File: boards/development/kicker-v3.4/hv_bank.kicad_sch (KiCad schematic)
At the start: 14 parts, among them Q3 BSS127S, Q4 AOD1N60

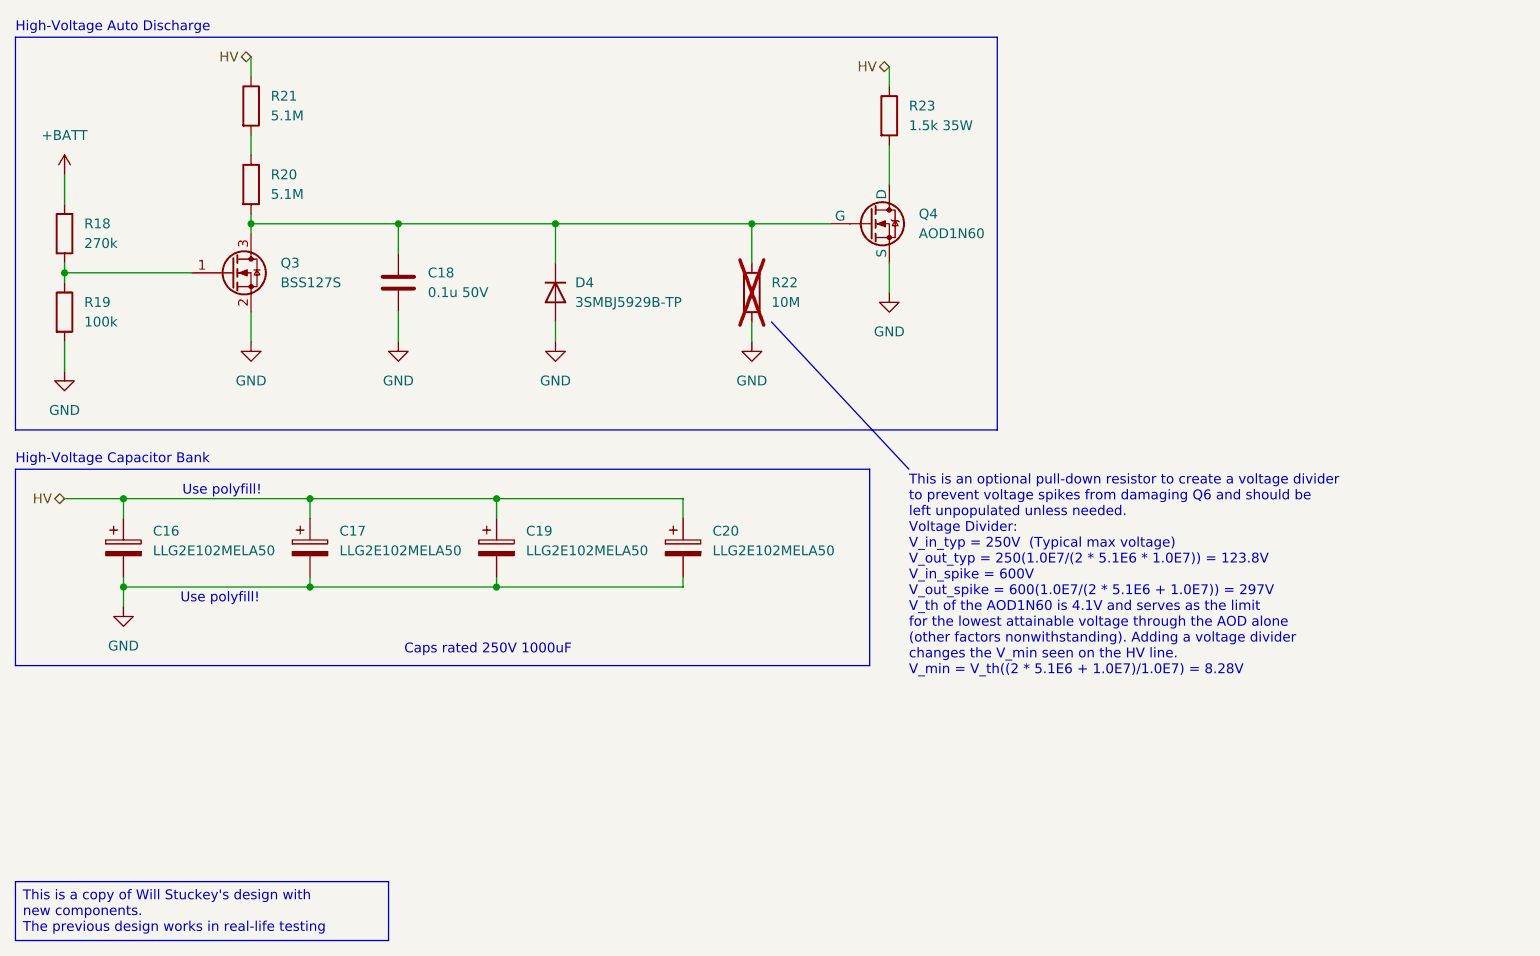
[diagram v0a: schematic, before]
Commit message: Add high voltage discharge
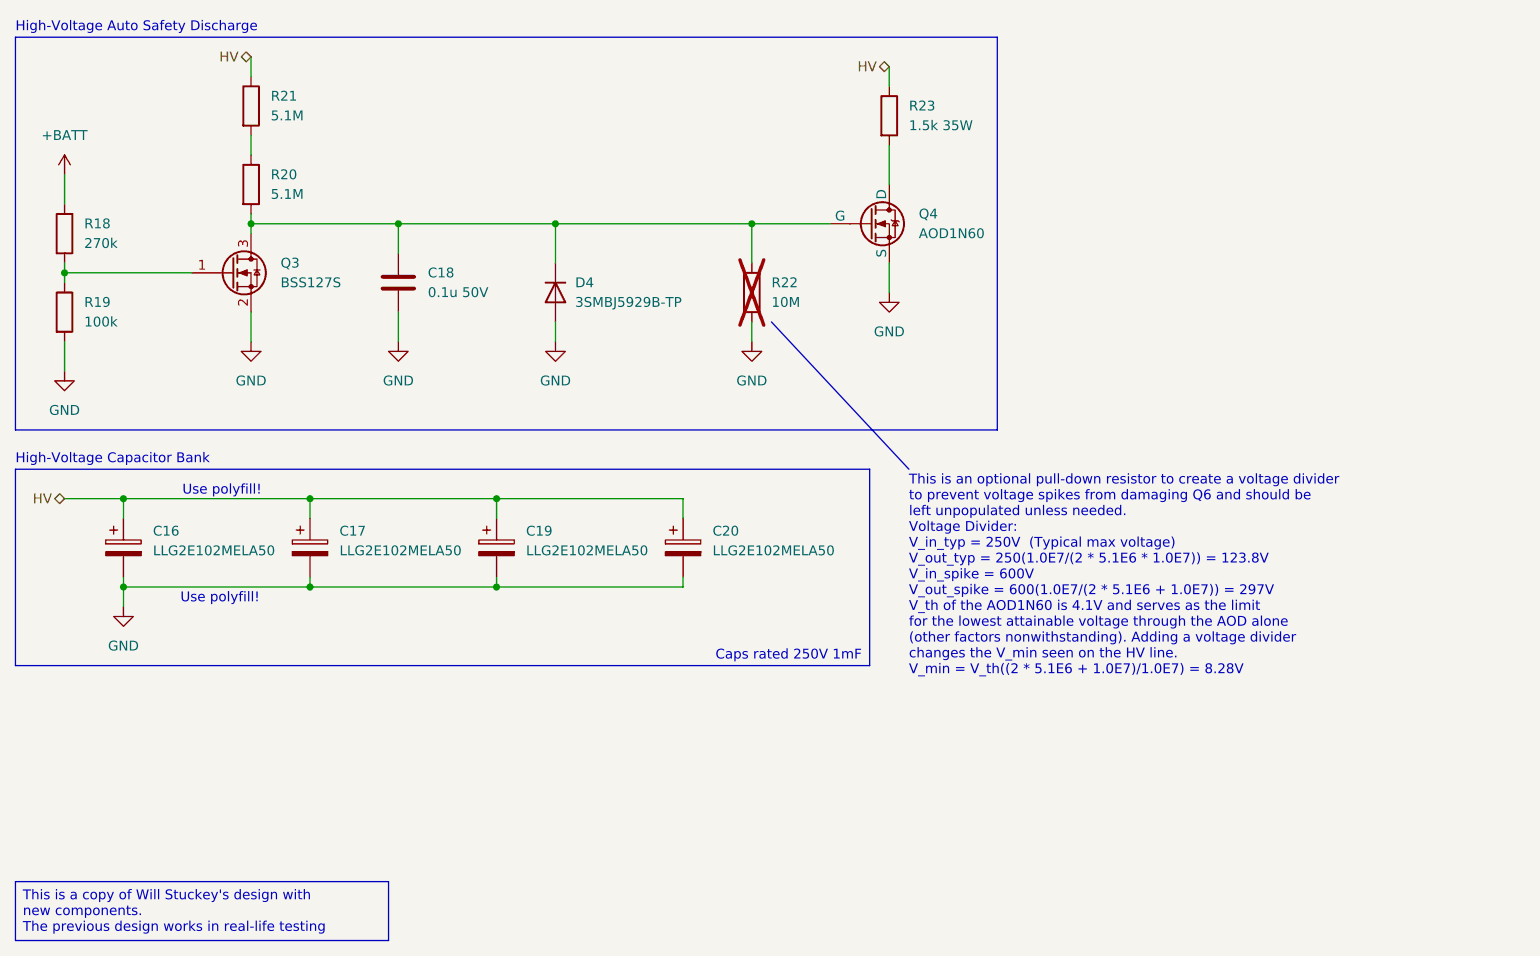
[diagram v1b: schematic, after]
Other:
- note added: "Caps rated 250V 1mF"
- note added: "High-Voltage Auto Safety Discharge"
- note removed: "Caps rated 250V 1000uF"
- note removed: "High-Voltage Auto Discharge"
- title: High Voltage Cap Bank w/ Auto Discharge -> High Voltage Cap Bank w/ Safety Auto Discharge
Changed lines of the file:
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@@
 	(paper "A5")
 	(title_block
-		(title "High Voltage Cap Bank w/ Auto Discharge")
+		(title "High Voltage Cap Bank w/ Safety Auto Discharge")
 		(rev "3.4-dev")
 		(company "RoboJackets - RoboCup")
@@
 		)
 	)
-	(text "Caps rated 250V 1000uF"
+	(text "Caps rated 250V 1mF"
 		(exclude_from_sim no)
-		(at 64.262 96.266 0)
+		(at 123.444 98.552 0)
 		(effects
 			(font
 				(size 1.27 1.27)
 			)
-			(justify left top)
+			(justify right bottom)
 		)
 	)
@@
 		)
 	)
-	(text "High-Voltage Auto Discharge"
+	(text "High-Voltage Auto Safety Discharge"
 		(exclude_from_sim no)
 		(at 13.97 17.272 0)

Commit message: Add MCU + debug features
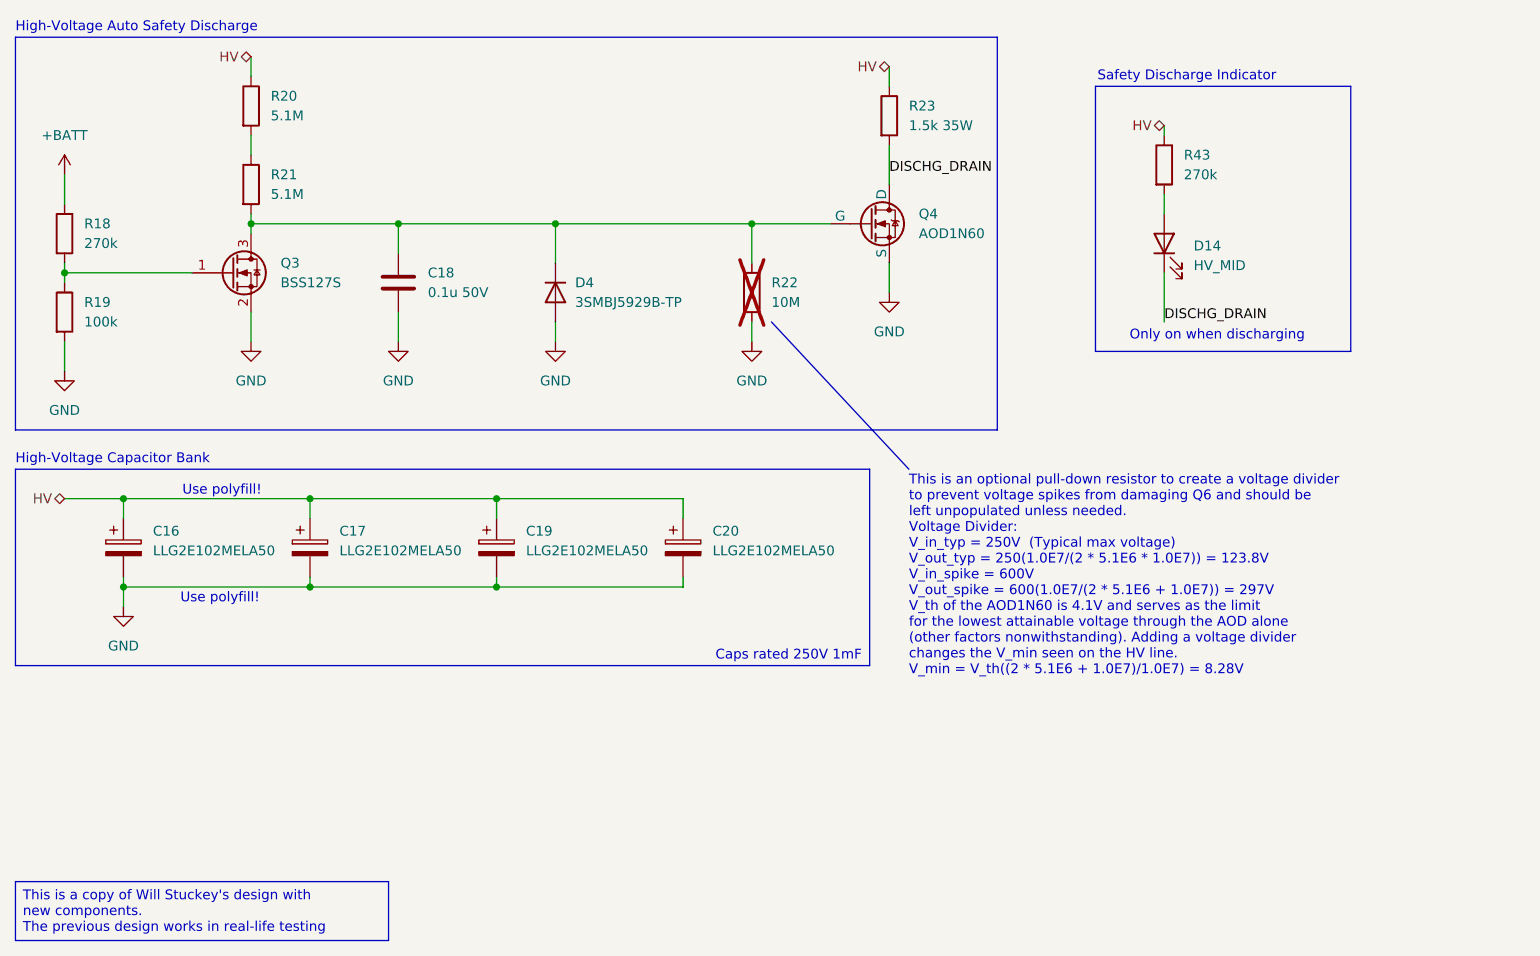
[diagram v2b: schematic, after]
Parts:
- added D14: HV_MID, LED_SMD:LED_0603_1608Metric, symbol Device:LED
- added R43: 270k, symbol Device:R
- renumbered R21 to R20, R20 to R21
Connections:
- net HV: now also R43.1
- net DISCHG_DRAIN: now reaches Q4.1 (D), R23.2
- net DISCHG_DRAIN: now also D14.1 (K)
- new net: D14.2 (A), R43.2
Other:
- note added: "Only on when discharging"
- note added: "Safety Discharge Indicator"
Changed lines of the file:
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@@
 	(title_block
 		(title "High Voltage Cap Bank w/ Safety Auto Discharge")
+		(date "2026-02-08")
 		(rev "3.4-dev")
 		(company "RoboJackets - RoboCup")
@@
 	)
 	(rectangle
+		(start 153.67 24.13)
+		(end 186.69 58.42)
+		(stroke
+			(width 0)
+			(type default)
+		)
+		(fill
+			(type none)
+		)
+	)
+	(rectangle
 		(start 13.97 73.66)
 		(end 124.46 99.06)
@@
 		(fill
 			(type none)
+		)
+	)
+	(text "Safety Discharge Indicator"
+		(exclude_from_sim no)
+		(at 153.924 23.622 0)
+		(effects
+			(font
+				(size 1.27 1.27)
+			)
+			(justify left bottom)
+		)
+	)
+	(text "Only on when discharging"
+		(exclude_from_sim no)
+		(at 169.418 57.15 0)
+		(effects
+			(font
+				(size 1.27 1.27)
+			)
+			(justify bottom)
 		)
 	)
@@
 	(wire
 		(pts
+			(xy 162.56 30.48) (xy 162.56 29.21)
+		)
+		(stroke
+			(width 0)
+			(type default)
+		)
+	)
+	(wire
+		(pts
 			(xy 76.2 77.47) (xy 76.2 80.01)
 		)
@@
 	(wire
 		(pts
+			(xy 162.56 38.1) (xy 162.56 40.64)
+		)
+		(stroke
+			(width 0)
+			(type default)
+		)
+	)
+	(wire
+		(pts
 			(xy 100.33 88.9) (xy 100.33 87.63)
 		)
@@
 	(wire
 		(pts
+			(xy 162.56 48.26) (xy 162.56 54.61)
+		)
+		(stroke
+			(width 0)
+			(type default)
+		)
+	)
+	(wire
+		(pts
 			(xy 100.33 77.47) (xy 100.33 80.01)
 		)
@@
 			(width 0)
 			(type default)
+		)
+	)
+	(label "DISCHG_DRAIN"
+		(at 127 35.56 0)
+		(effects
+			(font
+				(size 1.27 1.27)
+			)
+			(justify left bottom)
+		)
+	)
+	(label "DISCHG_DRAIN"
+		(at 162.56 54.61 0)
+		(effects
+			(font
+				(size 1.27 1.27)
+			)
+			(justify left bottom)
+		)
+	)
+	(hierarchical_label "HV"
+		(shape bidirectional)
+		(at 162.56 29.21 180)
+		(effects
+			(font
+				(size 1.27 1.27)
+			)
+			(justify right)
 		)
 	)
@@
 		(dnp no)
 		(fields_autoplaced yes)
-		(property "Reference" "R20"
+		(property "Reference" "R21"
 			(at 46.99 35.5599 0)
 			(effects
@@
 			(project "kicker-v3.4"
 				(path "/fb305a0d-eecf-446c-8807-75cb24f9e3a5/f4dc7313-c52c-44cc-8499-a4707a9c67a5"
-					(reference "R20")
+					(reference "R21")
 					(unit 1)
 				)
@@
 		(dnp no)
 		(fields_autoplaced yes)
-		(property "Reference" "#PWR037"
+		(property "Reference" "#PWR038"
 			(at 127 57.15 0)
 			(effects
@@
 			(project "kicker-v3.4"
 				(path "/fb305a0d-eecf-446c-8807-75cb24f9e3a5/f4dc7313-c52c-44cc-8499-a4707a9c67a5"
-					(reference "#PWR037")
+					(reference "#PWR038")
+					(unit 1)
+				)
+			)
+		)
+	)
+	(symbol
+		(lib_id "Device:R")
+		(at 162.56 34.29 0)
+		(unit 1)
+		(exclude_from_sim no)
+		(in_bom yes)
+		(on_board yes)
+		(dnp no)
+		(fields_autoplaced yes)
+		(property "Reference" "R43"
+			(at 165.1 33.0199 0)
+			(effects
+				(font
+					(size 1.27 1.27)
+				)
+				(justify left)
+			)
+		)
+		(property "Value" "270k"
+			(at 165.1 35.5599 0)
+			(effects
+				(font
+					(size 1.27 1.27)
+				)
+				(justify left)
+			)
+		)
+		(property "Footprint" ""
+			(at 160.782 34.29 90)
+			(effects
+				(font
+					(size 1.27 1.27)
+				)
+				(hide yes)
+			)
+		)
+		(property "Datasheet" "~"
+			(at 162.56 34.29 0)
+			(effects
+				(font
+					(size 1.27 1.27)
+				)
+				(hide yes)
+			)
+		)
+		(property "Description" "Resistor"
+			(at 162.56 34.29 0)
+			(effects
+				(font
+					(size 1.27 1.27)
+				)
+				(hide yes)
+			)
+		)
+		(pin "1"
+		)
+		(pin "2"
+		)
+		(instances
+			(project "kicker-v3.4"
+				(path "/fb305a0d-eecf-446c-8807-75cb24f9e3a5/f4dc7313-c52c-44cc-8499-a4707a9c67a5"
+					(reference "R43")
 					(unit 1)
 				)
@@
 		(dnp no)
 		(fields_autoplaced yes)
-		(property "Reference" "#PWR036"
+		(property "Reference" "#PWR037"
 			(at 109.22 63.5 0)
 			(effects
@@
 			(project "kicker-v3.4"
 				(path "/fb305a0d-eecf-446c-8807-75cb24f9e3a5/f4dc7313-c52c-44cc-8499-a4707a9c67a5"
-					(reference "#PWR036")
+					(reference "#PWR037")
 					(unit 1)
 				)
@@
 		(dnp no)
 		(fields_autoplaced yes)
-		(property "Reference" "#PWR034"
+		(property "Reference" "#PWR035"
 			(at 63.5 63.5 0)
 			(effects
@@
 			(project "kicker-v3.4"
 				(path "/fb305a0d-eecf-446c-8807-75cb24f9e3a5/f4dc7313-c52c-44cc-8499-a4707a9c67a5"
-					(reference "#PWR034")
+					(reference "#PWR035")
 					(unit 1)
 				)
@@
 		(dnp no)
 		(fields_autoplaced yes)
-		(property "Reference" "#PWR035"
+		(property "Reference" "#PWR036"
 			(at 83.82 63.5 0)
 			(effects
@@
 			(project "kicker-v3.4"
 				(path "/fb305a0d-eecf-446c-8807-75cb24f9e3a5/f4dc7313-c52c-44cc-8499-a4707a9c67a5"
-					(reference "#PWR035")
+					(reference "#PWR036")
 					(unit 1)
 				)
@@
 		(dnp no)
 		(fields_autoplaced yes)
-		(property "Reference" "#PWR033"
+		(property "Reference" "#PWR034"
 			(at 44.45 63.5 0)
 			(effects
@@
 			(project "kicker-v3.4"
 				(path "/fb305a0d-eecf-446c-8807-75cb24f9e3a5/f4dc7313-c52c-44cc-8499-a4707a9c67a5"
-					(reference "#PWR033")
+					(reference "#PWR034")
 					(unit 1)
 				)
@@
 		(dnp no)
 		(fields_autoplaced yes)
-		(property "Reference" "#PWR030"
+		(property "Reference" "#PWR033"
 			(at 27.94 97.79 0)
 			(effects
@@
 			(project ""
 				(path "/fb305a0d-eecf-446c-8807-75cb24f9e3a5/f4dc7313-c52c-44cc-8499-a4707a9c67a5"
-					(reference "#PWR030")
+					(reference "#PWR033")
 					(unit 1)
 				)
@@
 		(dnp no)
 		(fields_autoplaced yes)
-		(property "Reference" "R21"
+		(property "Reference" "R20"
 			(at 46.99 25.3999 0)
 			(effects
@@
 			(project "kicker-v3.4"
 				(path "/fb305a0d-eecf-446c-8807-75cb24f9e3a5/f4dc7313-c52c-44cc-8499-a4707a9c67a5"
-					(reference "R21")
-					(unit 1)
-				)
+					(reference "R20")
+					(unit 1)
+				)
+			)
+		)
+	)
+	(symbol
+		(lib_id "Device:LED")
+		(at 162.56 44.45 90)
+		(unit 1)
+		(exclude_from_sim no)
+		(in_bom yes)
+		(on_board yes)
+		(dnp no)
+		(fields_autoplaced yes)
+		(property "Reference" "D14"
+			(at 166.37 44.7674 90)
+			(effects
+				(font
+					(size 1.27 1.27)
+				)
+				(justify right)
+			)
+		)
+		(property "Value" "HV_MID"
+			(at 166.37 47.3074 90)
+			(effects
+				(font
+					(size 1.27 1.27)
+				)
+				(justify right)
+			)
+		)
+		(property "Footprint" "LED_SMD:LED_0603_1608Metric"
+			(at 162.56 44.45 0)
+			(effects
+				(font
+					(size 1.27 1.27)
+				)
+				(hide yes)
+			)
+		)
+		(property "Datasheet" "~"
+			(at 162.56 44.45 0)
+			(effects
+				(font
+					(size 1.27 1.27)
+				)
+				(hide yes)
+			)
+		)
+		(property "Description" "Light emitting diode"
+			(at 162.56 44.45 0)
+			(effects
+				(font
+					(size 1.27 1.27)
+				)
+				(hide yes)
+			)
+		)
+		(property "Sim.Pins" "1=K 2=A"
+			(at 162.56 44.45 0)
+			(effects
+				(font
+					(size 1.27 1.27)
+				)
+				(hide yes)
+			)
+		)
+		(pin "2"
+		)
+		(pin "1"
+		)
+		(instances
+			(project "kicker-v3.4"
+				(path "/fb305a0d-eecf-446c-8807-75cb24f9e3a5/f4dc7313-c52c-44cc-8499-a4707a9c67a5"
+					(reference "D14")
+					(unit 1)
+				)

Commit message: finish up footprint assignments
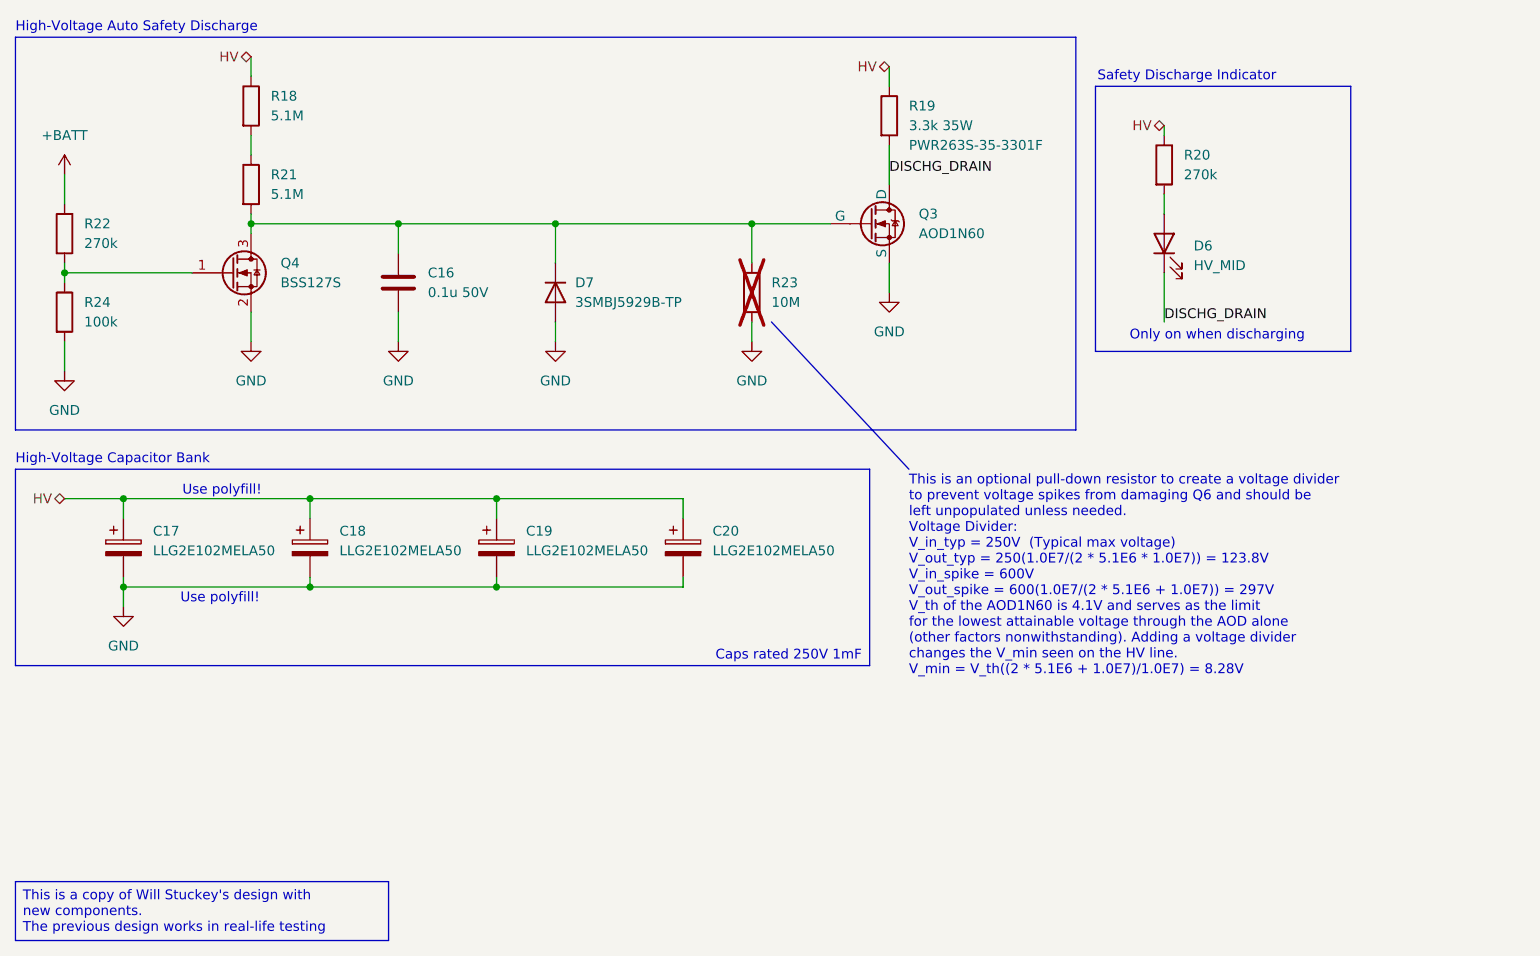
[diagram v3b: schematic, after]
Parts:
- removed C17: LLG2E102MELA50, symbol Device:C_Polarized
- added C18: LLG2E102MELA50, *piman_footprints:CP_A50_NCH, symbol Device:C_Polarized
- C16: renamed from C18; footprint (none) -> Capacitor_SMD:C_0603_1608Metric
- C17: renamed from C16; footprint (none) -> *piman_footprints:CP_A50_NCH
- C19, C20: footprint (none) -> *piman_footprints:CP_A50_NCH
- R18: renamed from R20; footprint (none) -> Resistor_SMD:R_0603_1608Metric
- R19: renamed from R23; value 1.5k 35W -> 3.3k 35W; footprint (none) -> *piman_footprints:RES_PWR263S-35-3301F; Manufacturer P/N (none) -> PWR263S-35-3301F; Vendor P/N (none) -> PWR263S-35-3301F-ND
- R20: renamed from R43; footprint (none) -> Resistor_SMD:R_0603_1608Metric
- R21: footprint (none) -> Resistor_SMD:R_0603_1608Metric
- R22: renamed from R18; footprint (none) -> Resistor_SMD:R_0603_1608Metric
- R23: renamed from R22; footprint (none) -> Resistor_SMD:R_0603_1608Metric
- R24: renamed from R19; footprint (none) -> Resistor_SMD:R_0603_1608Metric
- renumbered D14 to D6, D4 to D7, Q4 to Q3, Q3 to Q4
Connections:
- net GND: now also C18.2
- net HV: now also C18.1

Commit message: WIP Most placement done
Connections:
- net DISCHG_DRAIN: now also Q3.2 (D); no longer Q3.1 (D)
- net at C16.1, D7.2 (K), Q4.3 (D)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: now also Q3.1 (G); no longer Q3.2 (G)
